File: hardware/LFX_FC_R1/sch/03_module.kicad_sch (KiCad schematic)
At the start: 5 parts, among them J4 SM03B-SRSS-TB

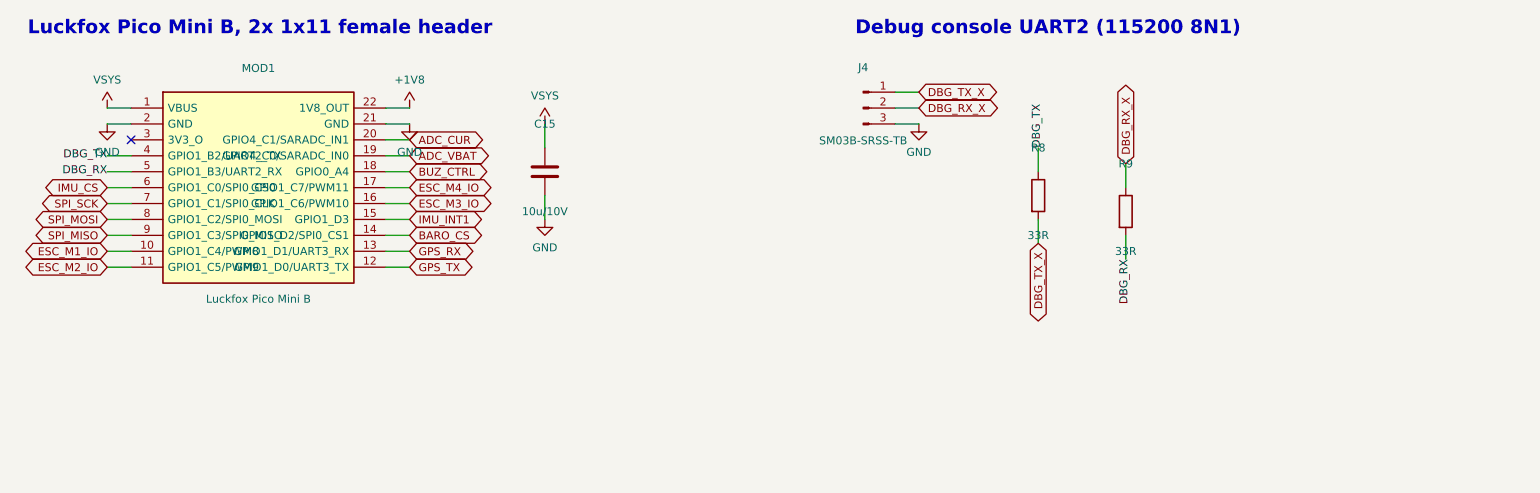
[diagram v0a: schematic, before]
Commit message: hardware: LFX_FC_R1 46x46 layout routed, DRC + parity clean
- 46 x 46 mm, M3 NPTH holes in the corners (39 x 39 mm pattern),
  JST-SH connectors on the edges, ESC S/G solder pads at the four corners
- IMU turned 90 deg so CS/SCK/MOSI/MISO face module pins 6..9 in order;
  the four lines are drawn (route_critical.hand_route_imu), not searched
- via/track keep-outs under the IMU and barometer bodies, 0.5 mm routing
  keep-out round the board rim
- EN divider re-laid as one column (U1.3 -> R1 -> R2 -> D2)
- VBAT divider top resistor moved to the battery end; only the divided
  node crosses the board
- GPS ESD at J5, series resistors at the module pins, no crossings
- router: hole-to-hole on same-net vias, 5 um freerouting clearance margin,
  off-plane fan-out vias removed
- schematic parity: global labels, library nicknames, MountingPin
  connectors, #FLG power flags, BOM exclusion for bare pads
- ERC 0, DRC 0 violations / 0 unconnected / 0 footprint errors
  (--schematic-parity)

Co-Authored-By: Claude Opus 5.5 <noreply@anthropic.com>
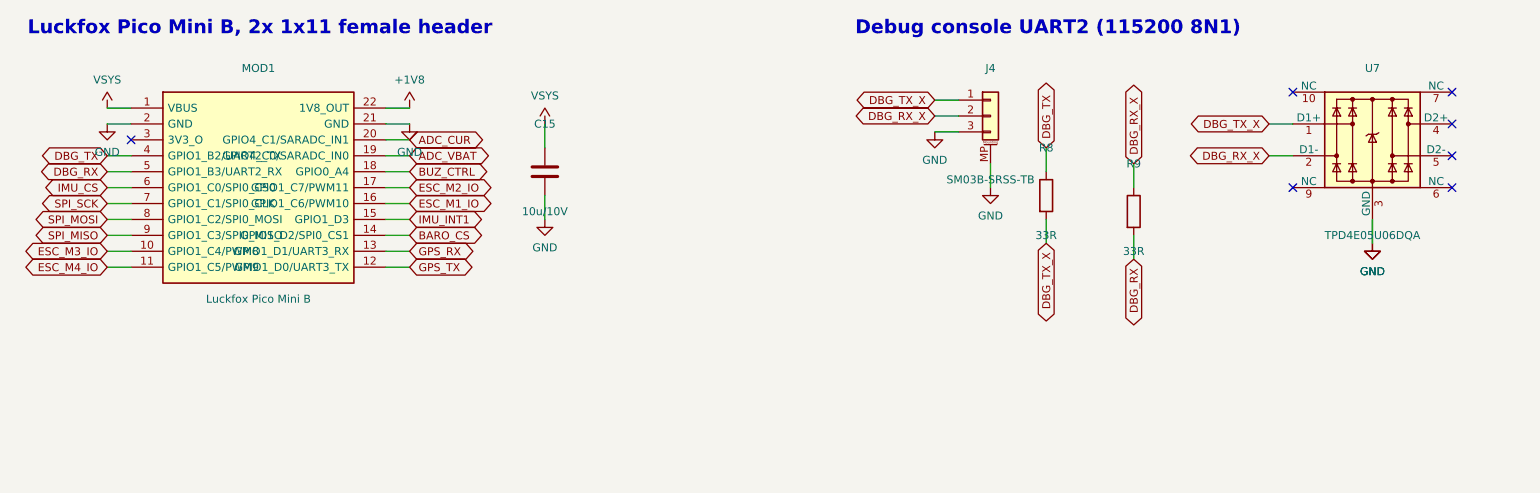
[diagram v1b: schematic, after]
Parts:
- added U7: TPD4E05U06DQA, Package_SON:USON-10_2.5x1.0mm_P0.5mm, symbol Power_Protection:TPD4E05U06DQA
- J4: symbol Connector:Conn_01x03_Pin -> Connector_Generic_MountingPin:Conn_01x03_MountingPin
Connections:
- net DBG_RX_X: now also U7.2 (D1-)
- net DBG_TX_X: now also U7.1 (D1+)
- net ESC_M1_IO: now also MOD1.16 (GPIO1_C6/PWM10); no longer MOD1.10 (GPIO1_C4/PWM8)
- net ESC_M2_IO: now also MOD1.17 (GPIO1_C7/PWM11); no longer MOD1.11 (GPIO1_C5/PWM9)
- net ESC_M3_IO: now also MOD1.10 (GPIO1_C4/PWM8); no longer MOD1.16 (GPIO1_C6/PWM10)
- net ESC_M4_IO: now also MOD1.11 (GPIO1_C5/PWM9); no longer MOD1.17 (GPIO1_C7/PWM11)
- net GND: now also J4.MP (MountPin), U7.3 (GND), U7.8 (GND)
- no-connect marks 1 -> 7
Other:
- moved on the sheet: J4, R8, R9

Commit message: hardware: RC receiver port (ELRS/CRSF) on UART2 instead of debug console
- J4 becomes a 4-pin JST-SH RC port: 1 5V, 2 GND, 3 TX (to receiver RX),
  4 RX (from receiver TX, CRSF 420000 baud), same order as the GPS port
- R24 1k pull-up on RC_RX to the module's 3V3 (pin 3): ESP-based ELRS
  receivers stall in the bootloader if that line is low at power-up
  (expresslrs.org receiver wiring guide)
- TP5/TP6 on RC_TX/RC_RX: console tap with the receiver unplugged
- UART2 has its own fractional divider (clk-rv1106.c:441), 420000 x 16 =
  24 MHz x 7/25; not yet measured
- docs: RC path goes through Linux, MCU failsafe on heartbeat loss; the
  console has to leave UART2 in software (fiq-debugger, earlycon)
- ERC 0, DRC 0 / 0 unconnected / 0 parity errors

Co-Authored-By: Claude Opus 5.5 <noreply@anthropic.com>
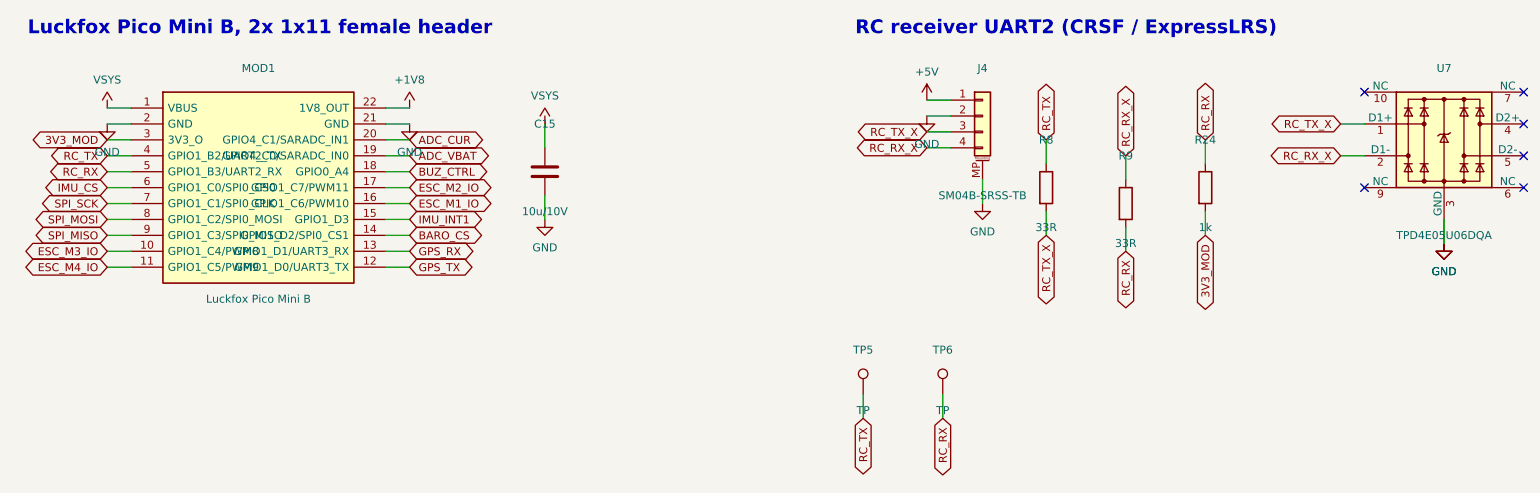
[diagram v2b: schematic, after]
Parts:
- added R24: 1k, Resistor_SMD:R_0402_1005Metric, symbol Device:R
- added TP5, TP6: TP, LFX:TestPad_1.0mm, symbol Connector:TestPoint
- J4: value SM03B-SRSS-TB -> SM04B-SRSS-TB; footprint Connector_JST:JST_SH_SM03B-SRSS-TB_1x03-1MP_P1.00mm_Horizontal -> Connector_JST:JST_SH_SM04B-SRSS-TB_1x04-1MP_P1.00mm_Horizontal; symbol Connector_Generic_MountingPin:Conn_01x03_MountingPin -> Connector_Generic_MountingPin:Conn_01x04_MountingPin
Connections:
- net GND: now also J4.2 (Pin_2); no longer J4.3 (Pin_3)
- net 3V3_MOD: now reaches MOD1.3 (3V3_O)
- net 3V3_MOD: now also R24.2
- net DBG_RX renamed RC_RX
- net RC_RX: now also R24.1, TP6.1
- net DBG_RX_X renamed RC_RX_X
- net RC_RX_X: now also J4.4 (Pin_4); no longer J4.2 (Pin_2)
- net DBG_TX renamed RC_TX
- net RC_TX: now also TP5.1
- net DBG_TX_X renamed RC_TX_X
- net RC_TX_X: now also J4.3 (Pin_3); no longer J4.1 (Pin_1)
- new net +5V: J4.1 (Pin_1)
- no-connect marks 7 -> 6
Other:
- note added: "RC receiver UART2 (CRSF / ExpressLRS)"
- note removed: "Debug console UART2 (115200 8N1)"
- moved on the sheet: R8, R9, U7

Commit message: hardware: LFX_LTE_R1 stacked LTE + GNSS board, FC link on J5
New 46 x 46 mm board hardware/LFX_LTE_R1 (same 39 mm M3 pattern, stacks on
the flight controller, all parts on the top side):
- Lierda NT26-KCN E LTE Cat.1 bis + GNSS (order the GPS + BDS variant);
  symbol and LCC/LGA-109 land pattern drawn from the Lierda hardware design
  manual Rev1.0 (table 2-5, fig. 2-2, fig. 8-3)
- TLV62569 buck +5V -> 3.8 V (modem VBAT 3.3-4.5 V), In2 +3V8 plane,
  2 x 47 uF + 100n / 33p / 8p2 at VBAT; TLV75533 3.3 V for the translators
- UART 3.3 <-> 1.8 V by 2 x SN74LVC1T45 (Hi-Z while the modem is off)
- Luckfox reflashes the modem: RESET_N via AO3400A, USB_BOOT via 1k from the
  1.8 V BOOT pin; USB / debug test pads for a PC rescue
- hinged nano-SIM with 22R / 33p / TPD4E05U06, LTE and GNSS U.FL with pi
  match, 50 ohm 0.35 mm feeds, active GNSS antenna bias
- ERC 0, DRC 0 violations / 0 unconnected / 0 parity

LFX_FC_R1 stays 46 x 46 mm:
- J5 GPS (JST-SH 4) -> LTE board link (JST-SH 10): 5V x2, GND x2, UART3,
  RESET (pin 18), BOOT (pin 20), buzzer gate, ESC current
- buzzer gate and ESC current now come from the modem's GPIO1 / ADC0
- ERC 0, DRC 0 violations / 0 unconnected / 0 parity

Shared: NT26-KCN and SIM_Card_Shield in the LFX library, stacked symbol
pins in gen_sch, route_pcb creates pcb/.  README and architecture docs
updated.

Co-Authored-By: Claude Opus 5.5 <noreply@anthropic.com>
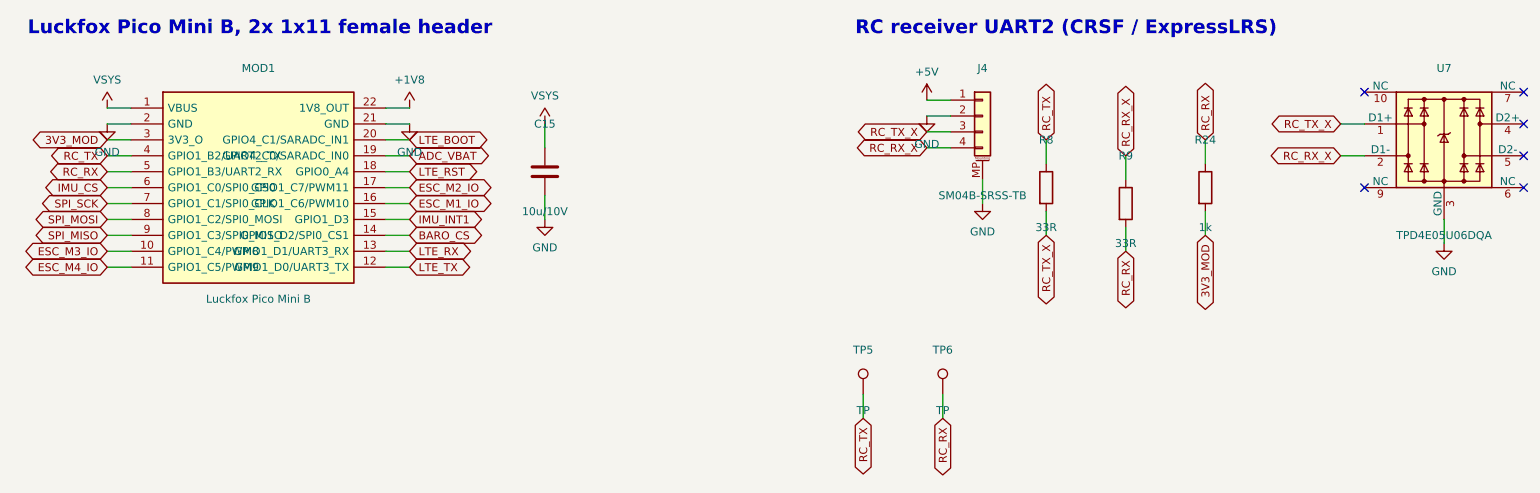
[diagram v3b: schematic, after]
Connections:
- net ADC_CUR renamed LTE_BOOT
- net BUZ_CTRL renamed LTE_RST
- net GPS_RX renamed LTE_RX
- net GPS_TX renamed LTE_TX
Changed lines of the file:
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@@
 		(stroke (width 0) (type default))
 	)
-	(global_label "ADC_CUR"
+	(global_label "LTE_BOOT"
 		(shape bidirectional)
 		(at 77.47 43.18 0)
@@
 		(stroke (width 0) (type default))
 	)
-	(global_label "BUZ_CTRL"
+	(global_label "LTE_RST"
 		(shape bidirectional)
 		(at 77.47 48.26 0)
@@
 		(stroke (width 0) (type default))
 	)
-	(global_label "GPS_RX"
+	(global_label "LTE_RX"
 		(shape bidirectional)
 		(at 77.47 60.96 0)
@@
 		(stroke (width 0) (type default))
 	)
-	(global_label "GPS_TX"
+	(global_label "LTE_TX"
 		(shape bidirectional)
 		(at 77.47 63.5 0)
@@
 		(at 255.27 35.56)
 	)
-	(wire
-		(pts (xy 242.57 55.88) (xy 242.57 59.69))
-		(stroke (width 0) (type default))
-	)
-	(symbol
-		(lib_id "power:GND")
-		(at 242.57 59.69 0)
-		(unit 1)
-		(exclude_from_sim no) (in_bom no) (on_board yes) (dnp no)
-		(property "Reference" "#PWR0061"
-			(at 242.57 55.88 0)
-			(effects (font (size 1.27 1.27)) (hide yes))
-		)
-		(property "Value" "GND"
-			(at 242.57 64.19 0)
-			(effects (font (size 1.27 1.27)))
-		)
-		(property "Footprint" "" (at 0 0 0) (effects (font (size 1.27 1.27)) (hide yes)))
-		(property "Datasheet" "" (at 0 0 0) (effects (font (size 1.27 1.27)) (hide yes)))
-		(instances
-			(project "LFX_FC_R1"
-				(path "/45fe5ea4-7ed3-d7ce-88f3-57d97f18bd10/cc2da1be-4875-9c97-002a-54558758a378"
-					(reference "#PWR0061") (unit 1)
-				)
-			)
-		)
-	)
 	(no_connect
